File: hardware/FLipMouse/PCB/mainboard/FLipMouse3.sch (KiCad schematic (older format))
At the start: 77 parts, among them J1 PJ320D, J10 Conn_01x06, J13 tp, J14 tp, J15 tp, J16 tp, J17 tp, J2 PJ320D, J3 M50-3900542, J4 Conn_ARM_JTAG_SWD_10, J5 Conn_02x05_Odd_Even, J9 USB_OTG, Q1 BC847, Q2 BSH108, Q3 BC847, Q4 BSH108, Q5 BSH108, Q6 BSH108, SW1 SW_Push, SW2 SW_Push, U1 ESP32-WROOM, U2 TSOP4838, U3 LPC11U14FBD, U4 TSR_1-2433, U5 MPXV7007GP, Y1 JA-12.000-18-DFE

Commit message: Schematic - beautify
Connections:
- wire segments 211 -> 208
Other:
- note added: "3V3 regulator"
- note added: "Analog Sensors"
- note added: "Decoupling ESP32"
- note added: "Decoupling LPC"
- note added: "ESP32 - auto-reset programming"
- note added: "ESP32 - main processor"
- note added: "Extension / I2C"
- note added: "Extension header"
- note added: "External Buttons"
- note added: "I2C pull-ups"
- note added: "IR TX (LEDs)"
- note added: "Infrared RX/TX"
- note added: "J13-J15 are used for \nUART ISP bootloader\n(together with ESP_RX/TX)"
- note added: "LPC - SWD debugging"
- note added: "Necessary to meet \nUSB specs in sleep\nmode current\nconsumption"
- note added: "Power Supply"
- note added: "PowerOff for ESP32"
- note added: "Pulldown - FSR"
- note added: "Sensor board connector"
- note added: "Sip/Puff"
- note added: "TSOP IR RX"
- note added: "User Input / Output"
- note removed: "3V3 regulator + power switch for ESP32"
- note removed: "7x external Jackplugs"
- note removed: "Decoupling for LPC & ESP32"
- note removed: "Designed like ESP32 Thing (Sparkfun)"
- note removed: "Programming interfaces"
- note removed: "TODO:\n- ESP32/LPC: mehr Leitungen (zweites IF?)\n- JackPlugs\n-ext header\n- LPC Notfallprogrammierung?"
- moved on the sheet: BZ1, C1, C10, C11, C12, C13, C14, C15, C16, C17, C18, C19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

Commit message: Changed component names for having all part types in one order. Added 3d shapes & beautified silkscreen layers.
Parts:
- R6: renamed from R1; value 1.5k -> 1k5
- R7: renamed from R4; value 1.5k -> 1k5
- renumbered C6 to C1, C17 to C10, C23 to C11, C22 to C13, C13 to C14, C19 to C16, C10 to C17, C16 to C18, C8 to C2, C1 to C3, C2 to C4, C11 to C5, C14 to C6, C18 to C7, C20 to C8, C21 to C9, D9 to D1, D3 to D2, D11 to D3, J9 to J6, J10 to J7, Q3 to Q2, Q2 to Q3, R9 to R1, R14 to R10, R17 to R11, R5 to R12, R6 to R13, R7 to R14, R8 to R15, R11 to R16, R22 to R17, R10 to R2, R21 to R20, R20 to R21, R12 to R22, R15 to R3, R16 to R4, R3 to R5, R2 to R8, R13 to R9, J13 to TP1, J14 to TP2, J15 to TP3, J16 to TP4, J17 to TP5

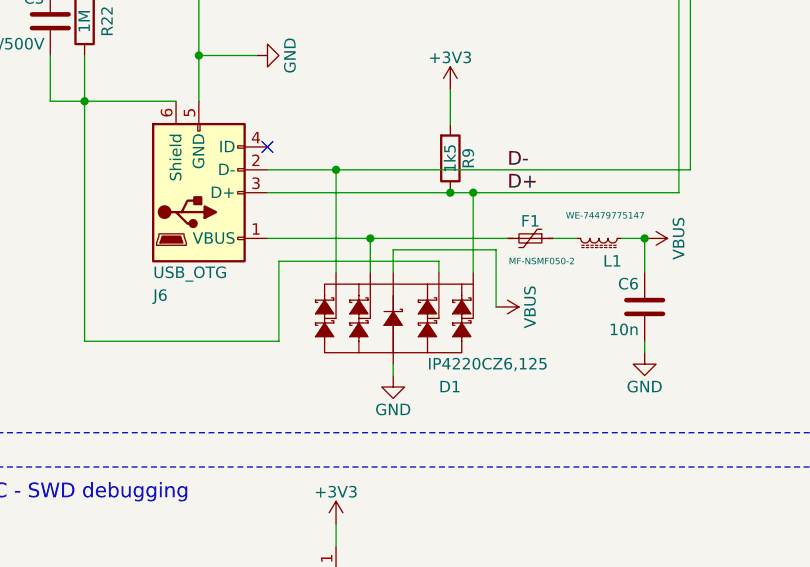
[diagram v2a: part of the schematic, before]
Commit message: Changed ESD protection for VBUS
Moved the supply voltage pin of suppressor diode array
from VBUS (after fuse & ferrite bead) to the power input of
the USB plug -> ESD protection is bad with an inductor limiting
the ESD diodes.
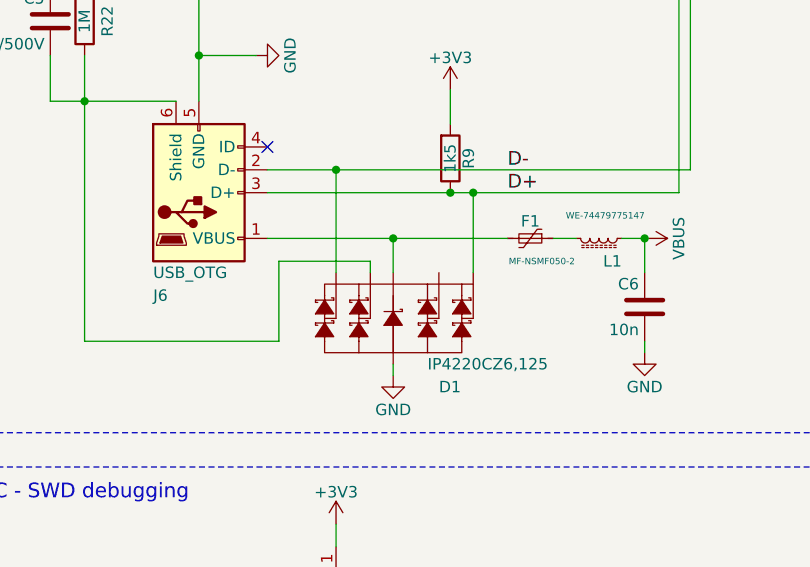
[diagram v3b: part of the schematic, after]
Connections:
- wire segments 208 -> 205
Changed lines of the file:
@@
 Connection ~ 2350 6950
 Wire Wire Line
-	2800 7400 2800 7350
-Wire Wire Line
-	2800 7350 2100 7350
+	2500 7350 2100 7350
 Wire Wire Line
 	2100 7350 2100 7700
@@
 EXT1
 Wire Wire Line
-	2050 7250 2500 7250
-Wire Wire Line
-	2500 7400 2500 7250
-Connection ~ 2500 7250
-Wire Wire Line
-	2500 7250 3100 7250
-Wire Wire Line
-	2600 7400 2600 7300
-Wire Wire Line
-	2600 7300 3050 7300
-Wire Wire Line
-	3050 7300 3050 7550
-$Comp
-L power:VBUS #PWR0119
-U 1 1 5C037606
-P 3050 7550
-F 0 "#PWR0119" H 3050 7400 50  0001 C CNN
-F 1 "VBUS" H 3050 7700 50  0000 C CNN
-F 2 "" H 3050 7550 50  0001 C CNN
-F 3 "" H 3050 7550 50  0001 C CNN
-	1    3050 7550
-	0    1    -1   0
-$EndComp
-Wire Wire Line
 	11500 1500 11500 2000
 Wire Wire Line
@@
 Wire Notes Line width 12 style solid
 	5150 10400 550  10400
+Wire Wire Line
+	2600 7250 2600 7400
+Connection ~ 2600 7250
+Wire Wire Line
+	2600 7250 3100 7250
+Wire Wire Line
+	2050 7250 2600 7250
+Wire Wire Line
+	2500 7350 2500 7400
 $EndSCHEMATC

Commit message: Production ready, alpha: * Added marks/logos/fiducials * Changed neopixel driving * Moved RX/TX of EXT header from internal UART to free pins * Renumbered all parts for having same part types with following numbers * Added PDFs of PCB
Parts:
- removed JP1: IO direct, Jumper:SolderJumper-2_P1.3mm_Open_Pad1.0x1.5mm, symbol Device:Jumper_NO_Small
- removed Q6: BSH108, Package_TO_SOT_SMD:SOT-23, symbol Device:Q_NMOS_GSD
- removed R10: 1k5, Resistor_SMD:R_0603_1608Metric, symbol Device:R
- added D8: 1N4148WS, Diode_SMD:D_SOD-323, symbol Device:D
- added FID1, FID2, FID3: Fiducial, Fiducial:Fiducial_0.5mm_Dia_1mm_Outer, symbol Mechanical:MountingHole
- added LOGO1: Logo_FLipMouse, Logo:flipmouse_11x5, symbol Mechanical:MountingHole
- added LOGO2: Logo_WEEE, Symbol:WEEE-Logo_4.2x6mm_SilkScreen, symbol Mechanical:MountingHole
- added LOGO3: Logo_CE, Logo:CE, symbol Mechanical:MountingHole
- C18: value 100uF -> 15uF
- R1, R2: value 22R,min 0.125W -> 15R,min 0.125W
- renumbered R11 to R10, R21 to R11, R22 to R21
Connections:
- net labels added: EXT_RX, EXT_TX
- wire segments 205 -> 198
- no-connect marks 46 -> 45
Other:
- note added: "Production"
- note removed: "route 3v3 directly\nto Neopixel"
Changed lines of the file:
@@
 Sheet 1 1
 Title "FLipMouse3"
-Date "2018-02-14"
+Date "2018-11-15"
 Rev "v3.1"
 Comp "AsTeRICS Foundation"
 Comment1 ""
-Comment2 ""
+Comment2 "Art. Number: 30310200"
 Comment3 "beni@asterics-foundation.org"
 Comment4 "(c) Benjamin Aigner, 2018"
@@
 $EndComp
 $Comp
-L Device:R R11
+L Device:R R10
 U 1 1 5A81C7FF
 P 13950 3100
-F 0 "R11" V 14030 3100 50  0000 C CNN
+F 0 "R10" V 14030 3100 50  0000 C CNN
 F 1 "1k5" V 13950 3100 50  0000 C CNN
 F 2 "Resistor_SMD:R_0603_1608Metric" V 13880 3100 50  0001 C CNN
@@
 $EndComp
 $Comp
-L Device:R R22
+L Device:R R21
 U 1 1 5A81D7F8
 P 1250 6300
-F 0 "R22" V 1350 6300 50  0000 C CNN
+F 0 "R21" V 1350 6300 50  0000 C CNN
 F 1 "1M" V 1250 6300 50  0000 C CNN
 F 2 "Resistor_SMD:R_0603_1608Metric" V 1180 6300 50  0001 C CNN
@@
 Text Label 6600 3000 2    60   ~ 0
 B_2
-Text Label 6600 2700 2    60   ~ 0
+Text Label 8450 2650 0    60   ~ 0
 B_0
 Text Label 6600 2900 2    60   ~ 0
@@
 Text Label 13700 1650 2    60   ~ 0
 LED1
-Text Label 9350 1700 0    60   ~ 0
+Text Label 8450 1950 0    60   ~ 0
 LED1
 $Comp
@@
 P 14800 5650
 F 0 "C18" H 14825 5750 50  0000 L CNN
-F 1 "100uF" H 14825 5550 50  0000 L CNN
+F 1 "15uF" H 14825 5550 50  0000 L CNN
 F 2 "Capacitor_Tantalum_SMD:CP_EIA-3216-18_Kemet-A" H 14838 5500 50  0001 C CNN
 F 3 "" H 14800 5650 50  0001 C CNN
@@
 P 14000 1650
 F 0 "D3" H 14200 1875 50  0000 R BNN
-F 1 "SK6812" V 13750 1900 50  0000 L TNN
+F 1 "SK6812" H 13600 1400 50  0000 L TNN
 F 2 "LED_SMD:LED_SK6812_PLCC4_5.0x5.0mm_P3.2mm" H 14050 1350 50  0001 L TNN
 F 3 "" H 14100 1275 50  0001 L TNN
@@
 L power:VBUS #PWR036
 U 1 1 5A8F25CB
-P 14000 1350
-F 0 "#PWR036" H 14000 1200 50  0001 C CNN
-F 1 "VBUS" H 14000 1500 50  0000 C CNN
-F 2 "" H 14000 1350 50  0001 C CNN
-F 3 "" H 14000 1350 50  0001 C CNN
-	1    14000 1350
-	1    0    0    -1
-$EndComp
-$Comp
-L power:GND #PWR037
-U 1 1 5A8F26CC
-P 14000 2050
-F 0 "#PWR037" H 14000 1800 50  0001 C CNN
-F 1 "GND" H 14000 1900 50  0000 C CNN
-F 2 "" H 14000 2050 50  0001 C CNN
-F 3 "" H 14000 2050 50  0001 C CNN
-	1    14000 2050
-	1    0    0    -1
-$EndComp
-$Comp
-L Device:Q_NMOS_GSD Q6
-U 1 1 5A8F367A
-P 9150 1900
-F 0 "Q6" H 9350 1950 50  0000 L CNN
-F 1 "BSH108" H 9350 1850 50  0000 L CNN
-F 2 "Package_TO_SOT_SMD:SOT-23" H 9350 2000 50  0001 C CNN
-F 3 "" H 9150 1900 50  0001 C CNN
-	1    9150 1900
-	1    0    0    -1
-$EndComp
-$Comp
-L power:GND #PWR038
-U 1 1 5A8F394D
-P 9250 2100
-F 0 "#PWR038" H 9250 1850 50  0001 C CNN
-F 1 "GND" H 9250 1950 50  0000 C CNN
-F 2 "" H 9250 2100 50  0001 C CNN
-F 3 "" H 9250 2100 50  0001 C CNN
-	1    9250 2100
-	1    0    0    -1
-$EndComp
-$Comp
-L Device:R R10
-U 1 1 5A8F3BAC
-P 9250 1550
-F 0 "R10" V 9330 1550 50  0000 C CNN
-F 1 "1k5" V 9250 1550 50  0000 C CNN
-F 2 "Resistor_SMD:R_0603_1608Metric" V 9180 1550 50  0001 C CNN
-F 3 "" H 9250 1550 50  0001 C CNN
-	1    9250 1550
-	1    0    0    -1
-$EndComp
-$Comp
-L power:VBUS #PWR039
-U 1 1 5A8F3E36
-P 9250 1300
-F 0 "#PWR039" H 9250 1150 50  0001 C CNN
-F 1 "VBUS" H 9250 1450 50  0000 C CNN
-F 2 "" H 9250 1300 50  0001 C CNN
-F 3 "" H 9250 1300 50  0001 C CNN
-	1    9250 1300
-	1    0    0    -1
+P 13650 1350
+F 0 "#PWR036" H 13650 1200 50  0001 C CNN
+F 1 "VBUS" H 13650 1500 50  0000 C CNN
+F 2 "" H 13650 1350 50  0001 C CNN
+F 3 "" H 13650 1350 50  0001 C CNN
+	1    13650 1350
+	0    -1   -1   0
 $EndComp
 $Comp
@@
 	13400 2250 13400 900
 Wire Notes Line
-	9850 4150 9850 900
-Wire Notes Line
-	9850 900  5500 900
+	9250 4150 9250 900
+Wire Notes Line
+	9250 900  5500 900
 Wire Notes Line
 	5500 900  5500 4150
 Wire Notes Line
-	5500 4150 9850 4150
+	5500 4150 9250 4150
 Wire Notes Line
 	14450 4150 13400 4150
@@
 	13400 4150 13400 2450
 Wire Wire Line
-	14000 2050 14000 1950
-Wire Wire Line
-	9250 1400 9250 1300
-Connection ~ 9250 1700
-Wire Wire Line
 	8950 2850 8450 2850
 Wire Wire Line
@@
 Wire Wire Line
 	3650 2100 3500 2100
-Wire Wire Line
-	8500 1900 8850 1900
-Wire Wire Line
-	8500 1900 8500 1950
-Wire Wire Line
-	8500 1950 8450 1950
 NoConn ~ 3500 4700
 Wire Wire Line
@@
 	5800 2100 6600 2100
 $Comp
-L Device:R R21
+L Device:R R11
 U 1 1 5B080FEC
 P 5800 1850
-F 0 "R21" V 5880 1850 50  0000 C CNN
+F 0 "R11" V 5880 1850 50  0000 C CNN
 F 1 "10k" V 5800 1850 50  0000 C CNN
 F 2 "Resistor_SMD:R_0603_1608Metric" V 5730 1850 50  0001 C CNN
@@
 Wire Wire Line
 	5800 2550 5800 2400
-$Comp
-L Device:Jumper_NO_Small JP1
-U 1 1 5B0839D4
-P 8950 1700
-F 0 "JP1" H 8950 1780 50  0000 C CNN
-F 1 "IO direct" H 8950 1850 50  0000 C CNN
-F 2 "Jumper:SolderJumper-2_P1.3mm_Open_Pad1.0x1.5mm" H 8950 1700 50  0001 C CNN
-F 3 "" H 8950 1700 50  0001 C CNN
-	1    8950 1700
-	1    0    0    -1
-$EndComp
 Wire Wire Line
 	6300 1750 6300 2000
 Wire Wire Line
-	9050 1700 9250 1700
-Wire Wire Line
-	8850 1900 8850 1700
-Connection ~ 8850 1900
-Text Notes 8900 1200 2    60   ~ 0
-route 3v3 directly\nto Neopixel
-Wire Wire Line
 	800  3250 800  3500
 Wire Wire Line
@@
 	1750 6450 1750 6650
 Wire Wire Line
-	9250 1700 9350 1700
-Wire Wire Line
 	2850 7050 2950 7050
 Wire Wire Line
@@
 Wire Wire Line
 	2950 7050 3850 7050
-Wire Wire Line
-	8850 1900 8950 1900
 Wire Wire Line
 	1250 6000 1750 6000
@@
 P 8850 6900
 F 0 "R1" H 8920 6946 50  0000 L CNN
-F 1 "22R,min 0.125W" H 9300 6700 50  0000 L CNN
+F 1 "15R,min 0.125W" H 9300 6700 50  0000 L CNN
 F 2 "Resistor_SMD:R_0603_1608Metric" V 8780 6900 50  0001 C CNN
 F 3 "~" H 8850 6900 50  0001 C CNN
@@
 P 9250 6900
 F 0 "R2" H 9320 6946 50  0000 L CNN
-F 1 "22R,min 0.125W" H 9300 6600 50  0000 L CNN
+F 1 "15R,min 0.125W" H 9300 6600 50  0000 L CNN
 F 2 "Resistor_SMD:R_0603_1608Metric" V 9180 6900 50  0001 C CNN
 F 3 "~" H 9250 6900 50  0001 C CNN
@@
 Text Label 15150 9300 0    60   ~ 0
 FSR4
-Text Label 8450 2650 0    60   ~ 0
+Text Label 6600 2700 2    60   ~ 0
 EXT1
 Text Label 5850 9250 3    60   ~ 0
@@
 Text Label 7750 9200 0    60   ~ 0
 EXT2
+Text Label 7250 9400 2    60   ~ 0
+EXT_TX
 Text Label 7750 9400 0    60   ~ 0
-ESP_TX
-Text Label 7250 9400 2    60   ~ 0
-ESP_RX
+EXT_RX
 NoConn ~ 11450 2800
 NoConn ~ 11600 2800
-NoConn ~ 8450 2950
 NoConn ~ 2850 9400
 $Comp
@@
 Text Label 8000 3650 3    60   ~ 0
 EXT2
-NoConn ~ 8450 2450
 NoConn ~ 11400 1400
 NoConn ~ 11400 1600
@@
 	1    0    0    -1
 $EndComp
-Wire Notes Line
-	8900 1250 8900 1500
-Wire Notes Line
-	8900 1500 8850 1450
-Wire Notes Line
-	8850 1450 8950 1450
-Wire Notes Line
-	8950 1450 8900 1500
 Wire Wire Line
 	4600 1150 4600 1400
@@
 	5350 9850 5350 8100
 Wire Notes Line width 12 style solid
-	10550 8100 10550 9850
+	5350 10050 5350 11050
 Wire Notes Line width 12 style solid
 	10550 8100 5350 8100
@@
 Wire Wire Line
 	2500 7350 2500 7400
+NoConn ~ 2800 7400
+$Comp
+L Device:D D8
+U 1 1 5C376CB2
+P 13850 1350
+F 0 "D8" H 13850 1134 50  0000 C CNN
+F 1 "1N4148WS" H 13850 1225 50  0000 C CNN
+F 2 "Diode_SMD:D_SOD-323" H 13850 1350 50  0001 C CNN
+F 3 "~" H 13850 1350 50  0001 C CNN
+	1    13850 1350
+	-1   0    0    1
+$EndComp
+$Comp
+L power:GNDD #PWR0119
+U 1 1 5C393ED2
+P 14000 2050
+F 0 "#PWR0119" H 14000 1800 50  0001 C CNN
+F 1 "GNDD" H 14000 1925 50  0000 C CNN
+F 2 "" H 14000 2050 50  0001 C CNN
+F 3 "" H 14000 2050 50  0001 C CNN
+	1    14000 2050
+	1    0    0    -1
+$EndComp
+Wire Wire Line
+	14000 2050 14000 1950
+Wire Wire Line
+	13650 1350 13700 1350
+Text Label 8450 2950 0    60   ~ 0
+EXT_TX
+Text Label 8450 2450 0    60   ~ 0
+EXT_RX
+$Comp
+L Mechanical:MountingHole LOGO1
+U 1 1 5C40D9CD
+P 6500 10500
+F 0 "LOGO1" H 6600 10546 50  0000 L CNN
+F 1 "Logo_FLipMouse" H 6600 10455 50  0000 L CNN
+F 2 "Logo:flipmouse_11x5" H 6500 10500 50  0001 C CNN
+F 3 "~" H 6500 10500 50  0001 C CNN
+	1    6500 10500
+	1    0    0    -1
+$EndComp
+$Comp
+L Mechanical:MountingHole LOGO2
+U 1 1 5C40DF40
+P 6500 10700
+F 0 "LOGO2" H 6600 10746 50  0000 L CNN
+F 1 "Logo_WEEE" H 6600 10655 50  0000 L CNN
+F 2 "Symbol:WEEE-Logo_4.2x6mm_SilkScreen" H 6500 10700 50  0001 C CNN
+F 3 "~" H 6500 10700 50  0001 C CNN
+	1    6500 10700
+	1    0    0    -1
+$EndComp
+$Comp
+L Mechanical:MountingHole LOGO3
+U 1 1 5C40DFF4
+P 6500 10900
+F 0 "LOGO3" H 6600 10946 50  0000 L CNN
+F 1 "Logo_CE" H 6600 10855 50  0000 L CNN
+F 2 "Logo:CE" H 6500 10900 50  0001 C CNN
+F 3 "~" H 6500 10900 50  0001 C CNN
+	1    6500 10900
+	1    0    0    -1
+$EndComp
+$Comp
+L Mechanical:MountingHole FID1
+U 1 1 5C41D5C3
+P 5950 10500
+F 0 "FID1" V 5904 10600 50  0000 L CNN
+F 1 "Fiducial" V 5995 10600 50  0000 L CNN
+F 2 "Fiducial:Fiducial_0.5mm_Dia_1mm_Outer" H 5950 10500 50  0001 C CNN
+F 3 "~" H 5950 10500 50  0001 C CNN
+	1    5950 10500
+	0    1    1    0
+$EndComp
+$Comp
+L Mechanical:MountingHole FID2
+U 1 1 5C42B940
+P 5950 10700
+F 0 "FID2" V 5904 10800 50  0000 L CNN
+F 1 "Fiducial" V 5995 10800 50  0000 L CNN
+F 2 "Fiducial:Fiducial_0.5mm_Dia_1mm_Outer" H 5950 10700 50  0001 C CNN
+F 3 "~" H 5950 10700 50  0001 C CNN
+	1    5950 10700
+	0    1    1    0
+$EndComp
+$Comp
+L Mechanical:MountingHole FID3
+U 1 1 5C42BA2C
+P 5950 10900
+F 0 "FID3" V 5904 11000 50  0000 L CNN
+F 1 "Fiducial" V 5995 11000 50  0000 L CNN
+F 2 "Fiducial:Fiducial_0.5mm_Dia_1mm_Outer" H 5950 10900 50  0001 C CNN
+F 3 "~" H 5950 10900 50  0001 C CNN
+	1    5950 10900
+	0    1    1    0
+$EndComp
+Wire Notes Line width 12 style solid
+	10550 8100 10550 9850
+Wire Notes Line width 12 style solid
+	8050 10050 8050 11050
+Wire Notes Line width 12 style solid
+	5350 10050 8050 10050
+Wire Notes Line width 12 style solid
+	5350 11050 8050 11050
+Text Notes 6150 10300 0    120  ~ 24
+Production
 $EndSCHEMATC

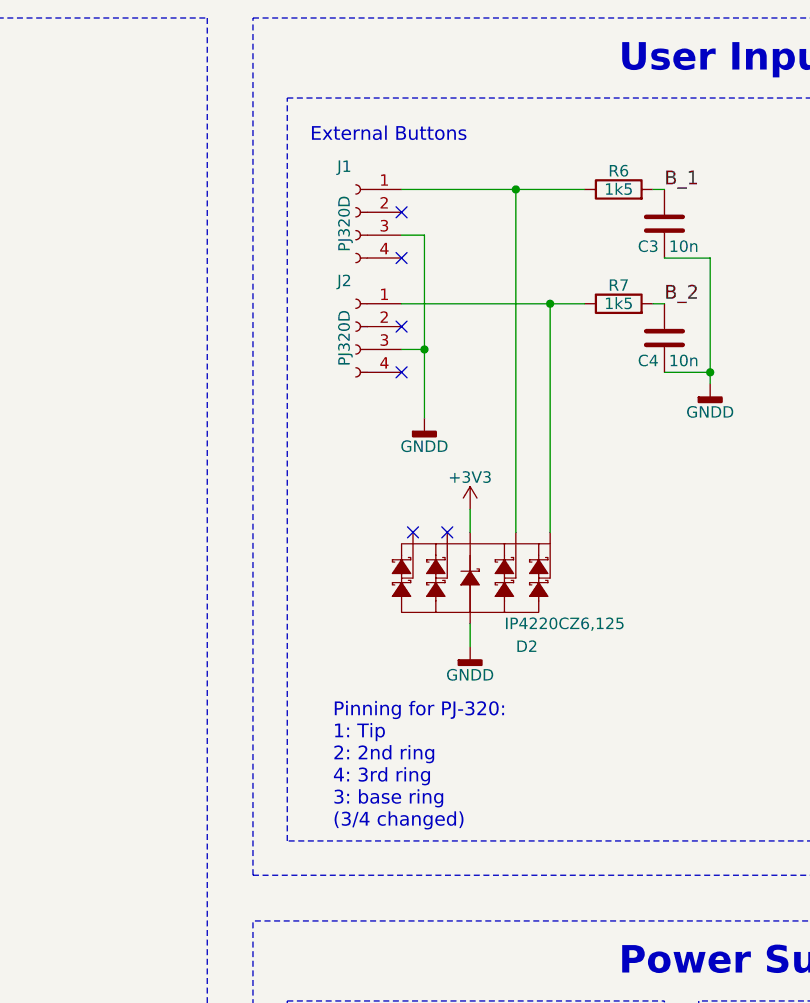
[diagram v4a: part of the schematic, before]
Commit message: Improvements&fixes: * Replaced PJ320D (china jack plugs) with plugs from digikey (RoHS!) * Added remaining 3D shapes to PCB * Removed GND from unused jack plug pins (might result in unusable buttons because of mono cables)
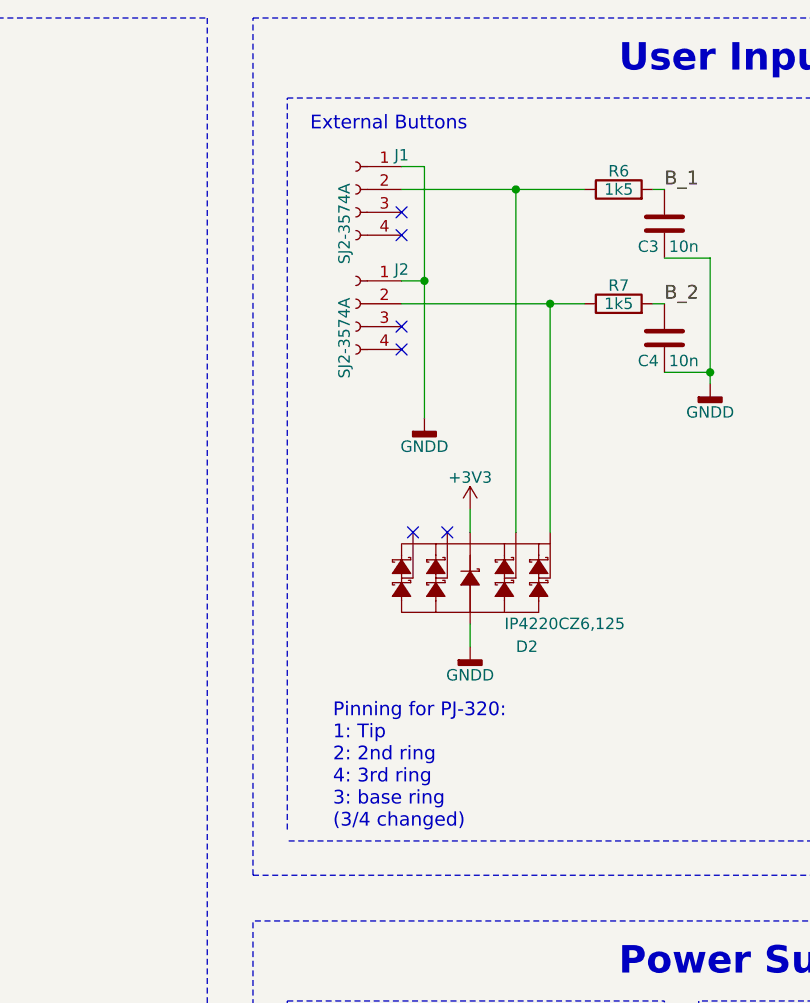
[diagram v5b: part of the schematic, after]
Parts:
- J1, J2: value PJ320D -> SJ2-3574A; footprint Connector_Audio:Jack_3.5mm_PJ320D_Horizontal -> JackPlug:Jack_3.5mm_SJ2-357X
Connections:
- net GNDD: now also J1.1 (Pin_1), J2.1 (Pin_1); no longer J1.3 (Pin_3), J2.3 (Pin_3)
- net at D2.6 (IO), R7.1: now also J2.2 (Pin_2); no longer J2.1 (Pin_1)
- net at D2.4 (IO), R6.1: now also J1.2 (Pin_2); no longer J1.1 (Pin_1)
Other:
- moved on the sheet: J1, J2
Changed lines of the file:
@@
 Text Notes 14200 5000 0    60   ~ 0
 Decoupling ESP32
-Text Notes 11000 1100 0    60   ~ 0
+Text Notes 11000 1050 0    60   ~ 0
 External Buttons
 Text Notes 12750 5000 0    60   ~ 0
@@
 	13200 4150 10900 4150
 Wire Notes Line
-	10900 4150 10900 900
+	10900 4100 10900 900
 Wire Notes Line
 	10900 900  13200 900
@@
 L Connector:Conn_01x04_Female J1
 U 1 1 5BF9CD2C
-P 11200 1400
-F 0 "J1" H 11250 1600 50  0000 C CNN
-F 1 "PJ320D" V 11250 1350 50  0000 C CNN
-F 2 "Connector_Audio:Jack_3.5mm_PJ320D_Horizontal" H 11200 1400 50  0001 C CNN
-F 3 "~" H 11200 1400 50  0001 C CNN
-	1    11200 1400
+P 11200 1300
+F 0 "J1" H 11000 1450 50  0000 C CNN
+F 1 "SJ2-3574A" V 11250 1150 50  0000 C CNN
+F 2 "JackPlug:Jack_3.5mm_SJ2-357X" H 11200 1300 50  0001 C CNN
+F 3 "~" H 11200 1300 50  0001 C CNN
+	1    11200 1300
 	-1   0    0    -1
 $EndComp
@@
 L Connector:Conn_01x04_Female J2
 U 1 1 5BF9D36C
-P 11200 1900
-F 0 "J2" H 11250 2100 50  0000 C CNN
-F 1 "PJ320D" V 11250 1850 50  0000 C CNN
-F 2 "Connector_Audio:Jack_3.5mm_PJ320D_Horizontal" H 11200 1900 50  0001 C CNN
-F 3 "~" H 11200 1900 50  0001 C CNN
-	1    11200 1900
+P 11200 1800
+F 0 "J2" H 11000 1950 50  0000 C CNN
+F 1 "SJ2-3574A" V 11250 1650 50  0000 C CNN
+F 2 "JackPlug:Jack_3.5mm_SJ2-357X" H 11200 1800 50  0001 C CNN
+F 3 "~" H 11200 1800 50  0001 C CNN
+	1    11200 1800
 	-1   0    0    -1
 $EndComp
@@
 	11400 1800 12050 1800
 Connection ~ 12050 1800
-Wire Wire Line
-	11400 1500 11500 1500
 $Comp
 L Connector_Generic:Conn_02x05_Odd_Even J3
@@
 Text Label 14650 9400 2    60   ~ 0
 EXT1
-Wire Wire Line
-	11500 1500 11500 2000
-Wire Wire Line
-	11400 2000 11500 2000
-Connection ~ 11500 2000
-Wire Wire Line
-	11500 2000 11500 2300
 Text Label 8000 3650 3    60   ~ 0
 EXT2
 NoConn ~ 11400 1400
-NoConn ~ 11400 1600
 NoConn ~ 11400 1900
-NoConn ~ 11400 2100
 NoConn ~ 8450 1850
 Wire Wire Line
@@
 Text Notes 6150 10300 0    120  ~ 24
 Production
+Wire Wire Line
+	11500 1200 11400 1200
+Wire Wire Line
+	11500 1200 11500 1700
+NoConn ~ 11400 1500
+Wire Wire Line
+	11400 1700 11500 1700
+Connection ~ 11500 1700
+Wire Wire Line
+	11500 1700 11500 2300
+NoConn ~ 11400 2000
 $EndSCHEMATC
